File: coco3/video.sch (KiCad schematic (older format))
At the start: 67 parts, among them CN3 Conn_02x05_Odd_Even, IC36 MC78L08_TO92, J5A1001 CVIDEO, J5B1001 SOUND, Q2 2SC945(NTE85), Q3 2SC945(NTE85), Q4 MPSA13(NTE46), Q5 2SC945(NTE85), Q6 2SC945(NTE85), Q7 2SC945(NTE85), SW3 SW3

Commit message: -replaced PIA's with he PLCC44 package versions -removed RF modulator -removed DRAM
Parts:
- removed C67: 10uF 25v, Capacitor_THT:CP_Radial_D5.0mm_P2.00mm, symbol Device:CP_Small
- removed R26: 2.2K, Resistor_THT:R_Axial_DIN0207_L6.3mm_D2.5mm_P10.16mm_Horizontal, symbol Device:R_Small_US
- removed R60: 100, Resistor_THT:R_Axial_DIN0207_L6.3mm_D2.5mm_P10.16mm_Horizontal, symbol Device:R_Small_US
- removed RF1: CoCo3RFModulator, coco2:CoCo 3 RF Modulator, symbol coco2:CoCo3RFModulator
- removed SW3: SW3, coco2:SW_EG1213, symbol Switch:SW_SPDT
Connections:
- net labels removed: CH, S, V
- wire segments 195 -> 171
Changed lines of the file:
@@
 	0    -1   -1   0
-$EndComp
-Wire Wire Line
-	6650 4150 6650 4300
-Wire Wire Line
-	6400 4150 6650 4150
-Wire Wire Line
-	6400 4000 6400 4150
-$Comp
-L power:GNDS #PWR?
-U 1 1 61184351
-P 6650 4300
-AR Path="/602A51A8/61184351" Ref="#PWR?"  Part="1"
-AR Path="/60308A73/61184351" Ref="#PWR?"  Part="1"
-AR Path="/603E4732/61184351" Ref="#PWR?"  Part="1"
-AR Path="/603D345E/61184351" Ref="#PWR?"  Part="1"
-AR Path="/61184351" Ref="#PWR?"  Part="1"
-AR Path="/612A4892/61184351" Ref="#PWR01104"  Part="1"
-F 0 "#PWR01104" H 6650 4050 50  0001 C CNN
-F 1 "GNDS" H 6650 4150 50  0000 C CNN
-F 2 "" H 6650 4300 50  0001 C CNN
-F 3 "" H 6650 4300 50  0001 C CNN
-	1    6650 4300
-	1    0    0    -1
-$EndComp
-Wire Wire Line
-	6200 4450 6200 4000
-Wire Wire Line
-	6000 4450 6200 4450
-$Comp
-L Device:R_Small_US R?
-U 1 1 6116CABF
-P 5900 4450
-AR Path="/60273794/6116CABF" Ref="R?"  Part="1"
-AR Path="/603D560B/6116CABF" Ref="R?"  Part="1"
-AR Path="/603CF7B8/6116CABF" Ref="R?"  Part="1"
-AR Path="/612A4892/6116CABF" Ref="R60"  Part="1"
-F 0 "R60" V 6000 4400 50  0000 L CNN
-F 1 "100" V 5800 4400 50  0000 L CNN
-F 2 "Resistor_THT:R_Axial_DIN0207_L6.3mm_D2.5mm_P10.16mm_Horizontal" H 5900 4450 50  0001 C CNN
-F 3 " https://www.seielect.com/catalog/sei-cf_cfm.pdf" H 5900 4450 50  0001 C CNN
-F 4 "digikey" H 5900 4450 50  0001 C CNN "Vendor"
-F 5 "CF14JT100RCT-ND" H 5900 4450 50  0001 C CNN "Vendor part#"
-F 6 "CF14JT100R" H 5900 4450 50  0001 C CNN "Manufacturer part#"
-	1    5900 4450
-	0    -1   -1   0
-$EndComp
-$Comp
-L Switch:SW_SPDT SW3
-U 1 1 6113439A
-P 6300 3800
-F 0 "SW3" V 6254 3948 50  0000 L CNN
-F 1 "SW3" V 6345 3948 50  0000 L CNN
-F 2 "coco2:SW_EG1213" H 6300 3800 50  0001 C CNN
-F 3 "https://sten-eswitch-13110800-production.s3.amazonaws.com/system/asset/product_line/data_sheet/119/EG.pdf" H 6300 3800 50  0001 C CNN
-F 4 "digikey" H 6300 3800 50  0001 C CNN "Vendor"
-F 5 "EG1906-ND" H 6300 3800 50  0001 C CNN "Vendor part#"
-F 6 "EG1213" H 6300 3800 50  0001 C CNN "Manufacturer part#"
-	1    6300 3800
-	0    -1   1    0
 $EndComp
 Connection ~ 4550 4950
@@
 	1    0    0    -1
 $EndComp
-Connection ~ 4550 6400
-Wire Wire Line
-	4550 6600 4550 6400
-$Comp
-L power:GNDS #PWR?
-U 1 1 61305ADB
-P 4550 6950
-AR Path="/602A51A8/61305ADB" Ref="#PWR?"  Part="1"
-AR Path="/60308A73/61305ADB" Ref="#PWR?"  Part="1"
-AR Path="/603E4732/61305ADB" Ref="#PWR?"  Part="1"
-AR Path="/603D345E/61305ADB" Ref="#PWR?"  Part="1"
-AR Path="/61305ADB" Ref="#PWR?"  Part="1"
-AR Path="/612A4892/61305ADB" Ref="#PWR01103"  Part="1"
-F 0 "#PWR01103" H 4550 6700 50  0001 C CNN
-F 1 "GNDS" H 4550 6800 50  0000 C CNN
-F 2 "" H 4550 6950 50  0001 C CNN
-F 3 "" H 4550 6950 50  0001 C CNN
-	1    4550 6950
-	1    0    0    -1
-$EndComp
-$Comp
-L Device:R_Small_US R?
-U 1 1 61302455
-P 4550 6700
-AR Path="/60273794/61302455" Ref="R?"  Part="1"
-AR Path="/603D560B/61302455" Ref="R?"  Part="1"
-AR Path="/603CF7B8/61302455" Ref="R?"  Part="1"
-AR Path="/612A4892/61302455" Ref="R26"  Part="1"
-F 0 "R26" H 4650 6700 50  0000 L CNN
-F 1 "2.2K" H 4600 6800 50  0000 L CNN
-F 2 "Resistor_THT:R_Axial_DIN0207_L6.3mm_D2.5mm_P10.16mm_Horizontal" H 4550 6700 50  0001 C CNN
-F 3 "https://www.seielect.com/catalog/sei-cf_cfm.pdf" H 4550 6700 50  0001 C CNN
-F 4 "digikey" H 4550 6700 50  0001 C CNN "Vendor"
-F 5 "CF14JT2K20CT-ND" H 4550 6700 50  0001 C CNN "Vendor part#"
-F 6 "CF14JT2K20" H 4550 6700 50  0001 C CNN "Manufacturer part#"
-	1    4550 6700
-	-1   0    0    1
-$EndComp
-Wire Wire Line
-	3850 6400 4550 6400
-$Comp
-L Device:CP_Small C?
-U 1 1 612EE250
-P 3750 6400
-AR Path="/60273794/612EE250" Ref="C?"  Part="1"
-AR Path="/612A4892/612EE250" Ref="C67"  Part="1"
-F 0 "C67" V 4000 6400 50  0000 C CNN
-F 1 "10uF 25v" V 3850 6400 50  0000 C CNN
-F 2 "Capacitor_THT:CP_Radial_D5.0mm_P2.00mm" H 3750 6400 50  0001 C CNN
-F 3 "http://nichicon-us.com/english/products/pdfs/e-upw.pdf" H 3750 6400 50  0001 C CNN
-F 4 "digikey" V 3750 6400 50  0001 C CNN "Vendor"
-F 5 "493-1809-ND" V 3750 6400 50  0001 C CNN "Vendor part#"
-F 6 "UPW1E100MDD" V 3750 6400 50  0001 C CNN "Manufacturer part#"
-	1    3750 6400
-	0    -1   -1   0
-$EndComp
-Connection ~ 7500 2400
-Wire Wire Line
-	7500 2400 7050 2400
 Wire Wire Line
 	7550 2200 7250 2200
@@
 Wire Wire Line
 	4000 2250 3750 2250
-$Comp
-L coco2:CoCo3RFModulator RF1
-U 1 1 6110FA77
-P 7900 2950
-F 0 "RF1" H 7850 2750 50  0000 L CNN
-F 1 "CoCo3RFModulator" V 8150 2150 50  0000 L CNN
-F 2 "coco2:CoCo 3 RF Modulator" H 7900 2950 50  0001 C CNN
-F 3 "" H 7900 2950 50  0001 C CNN
-	1    7900 2950
-	1    0    0    -1
-$EndComp
-Wire Wire Line
-	4550 6800 4550 6950
-Wire Wire Line
-	4950 4450 5800 4450
 Wire Wire Line
 	4000 2250 4750 2250
-Wire Wire Line
-	4000 2250 4000 3350
-Wire Wire Line
-	4000 3350 2600 3350
-Wire Wire Line
-	2600 3350 2600 6400
-Wire Wire Line
-	2600 6400 3650 6400
-Wire Wire Line
-	7050 2400 7050 3300
-Wire Wire Line
-	7050 3300 7600 3300
-Wire Wire Line
-	6300 3400 6300 3600
-Wire Wire Line
-	6300 3400 7600 3400
-Text GLabel 7400 3500 0    50   Output ~ 0
-8V
-Wire Wire Line
-	7400 3500 7600 3500
-Wire Wire Line
-	6900 6400 6900 3600
-Wire Wire Line
-	6900 3600 7600 3600
-Wire Wire Line
-	4550 6400 6900 6400
-$Comp
-L power:GNDS #PWR?
-U 1 1 61354D89
-P 7350 3800
-AR Path="/602A51A8/61354D89" Ref="#PWR?"  Part="1"
-AR Path="/60308A73/61354D89" Ref="#PWR?"  Part="1"
-AR Path="/603E4732/61354D89" Ref="#PWR?"  Part="1"
-AR Path="/603D345E/61354D89" Ref="#PWR?"  Part="1"
-AR Path="/61354D89" Ref="#PWR?"  Part="1"
-AR Path="/612A4892/61354D89" Ref="#PWR0109"  Part="1"
-F 0 "#PWR0109" H 7350 3550 50  0001 C CNN
-F 1 "GNDS" H 7350 3650 50  0000 C CNN
-F 2 "" H 7350 3800 50  0001 C CNN
-F 3 "" H 7350 3800 50  0001 C CNN
-	1    7350 3800
-	1    0    0    -1
-$EndComp
-Wire Wire Line
-	7600 3700 7350 3700
-Wire Wire Line
-	7350 3700 7350 3800
-Text Label 7400 3300 0    50   ~ 0
-S
-Text Label 7400 3400 0    50   ~ 0
-CH
-Text Label 7450 3600 0    50   ~ 0
-V
 $EndSCHEMATC

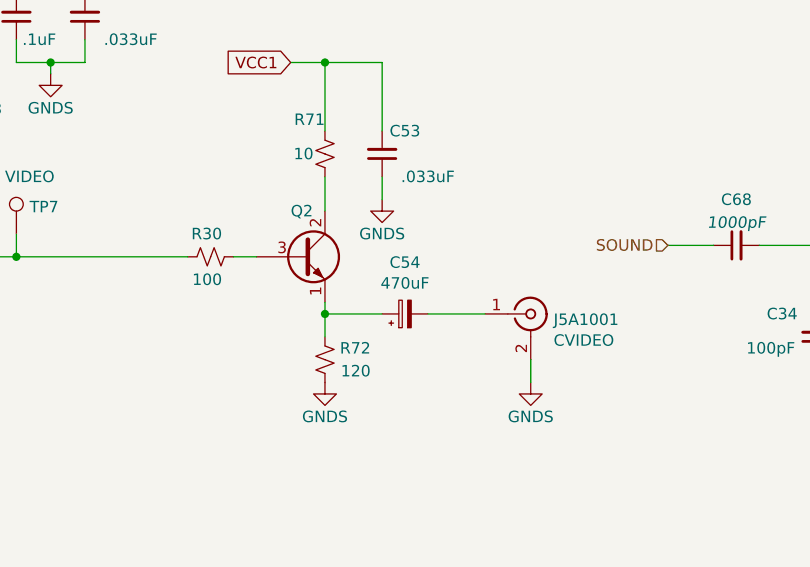
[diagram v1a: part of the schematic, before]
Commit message: -repplaced a whole bunch of THT components with SMT components
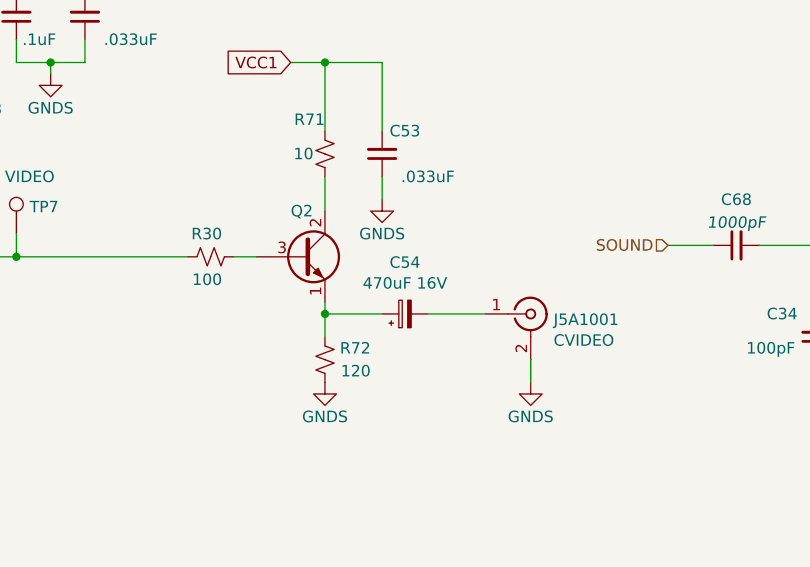
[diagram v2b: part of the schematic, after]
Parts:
- C34: footprint Capacitor_THT:C_Disc_D4.3mm_W1.9mm_P5.00mm -> Capacitor_SMD:C_0805_2012Metric_Pad1.18x1.45mm_HandSolder; Manufacturer part# K101J15C0GF5TH5 -> CL21C101JBANNNC; Vendor digikey -> JLCPCB; Vendor part# BC1042CT-ND -> C1790
- C37: footprint Capacitor_THT:C_Disc_D4.7mm_W2.5mm_P5.00mm -> Capacitor_SMD:C_0805_2012Metric_Pad1.18x1.45mm_HandSolder; Manufacturer part# K390J15C0GF5TL2 -> 0805N390J500CT; Vendor digikey -> JLCPCB; Vendor part# BC1008CT-ND -> C296098
- C42, C50, C51: footprint Capacitor_THT:C_Disc_D4.7mm_W2.5mm_P5.00mm -> Capacitor_SMD:C_0805_2012Metric_Pad1.18x1.45mm_HandSolder; Manufacturer part# FG28C0G1H103JNT06 -> CL21A106KAYNNNE; Vendor digikey -> JLCPCB; Vendor part# 445-173474-1-ND -> C15850
- C52, C53: footprint Capacitor_THT:C_Axial_L5.1mm_D3.1mm_P10.00mm_Horizontal -> Capacitor_SMD:C_0805_2012Metric_Pad1.18x1.45mm_HandSolder; Manufacturer part# C410C333K5R5TA7200 -> 0805B333K500NT; Vendor digikey -> JLCPCB; Vendor part# 399-4470-1-ND -> C1739
- C54: value 470uF -> 470uF 16V; footprint Capacitor_THT:CP_Radial_D8.0mm_P3.50mm -> Capacitor_SMD:CP_Elec_8x10; Manufacturer part# ECA-1CM471 -> VEJ471M1CTR-0810; Vendor digikey -> JLCPCB; Vendor part# P5141-ND -> C176671
- C55, C56: footprint Capacitor_THT:CP_Radial_D5.0mm_P2.00mm -> Capacitor_SMD:CP_Elec_4x5.3; Manufacturer part# UPW1E100MDD -> VE-100M1ETR-0405; Vendor digikey -> JLCPCB; Vendor part# 493-1809-ND -> C134721
- C57: footprint Capacitor_THT:C_Axial_L5.1mm_D3.1mm_P10.00mm_Horizontal -> Capacitor_SMD:C_0805_2012Metric_Pad1.18x1.45mm_HandSolder; Manufacturer part# C410C223K5R5TA7200 -> CL21B223KBANNNC; Vendor digikey -> JLCPCB; Vendor part# 399-4464-1-ND -> C1729
- C58, C59, C68: footprint Capacitor_THT:C_Disc_D4.7mm_W2.5mm_P5.00mm -> Capacitor_SMD:C_0805_2012Metric_Pad1.18x1.45mm_HandSolder; Manufacturer part# K102K10X7RF5UH5 -> CL21B102KBCNNNC; Vendor digikey -> JLCPCB; Vendor part# BC2659CT-ND -> C46653
- C62, C63: footprint Capacitor_THT:CP_Radial_D8.0mm_P3.50mm -> Capacitor_SMD:CP_Elec_8x10; Manufacturer part# ECA-1EM221 -> VEJ221M1ETR-0810; Vendor digikey -> JLCPCB; Vendor part# P5153-ND -> C134765
- R28, R39, R46, R53, R68, R71: footprint Resistor_THT:R_Axial_DIN0207_L6.3mm_D2.5mm_P10.16mm_Horizontal -> Resistor_SMD:R_1206_3216Metric_Pad1.30x1.75mm_HandSolder; Manufacturer part# CFR-25JB-52-10R -> 1206W4F100JT5E; Vendor digikey -> JLCPCB; Vendor part# 10QBK-ND -> C17903
- R30, R34, R69: footprint Resistor_THT:R_Axial_DIN0207_L6.3mm_D2.5mm_P10.16mm_Horizontal -> Resistor_SMD:R_1206_3216Metric_Pad1.30x1.75mm_HandSolder; Manufacturer part# CF14JT100R -> 1206W4F1000T5E; Vendor digikey -> JLCPCB; Vendor part# CF14JT100RCT-ND -> C17901
- R33, R35: footprint Resistor_THT:R_Axial_DIN0207_L6.3mm_D2.5mm_P10.16mm_Horizontal -> Resistor_SMD:R_1206_3216Metric_Pad1.30x1.75mm_HandSolder; Manufacturer part# CF14JT220K -> 1206W4F2203T5E; Vendor digikey -> JLCPCB; Vendor part# CF14JT220KCT-ND -> C17956
- R36, R40, R47, R54: footprint Resistor_THT:R_Axial_DIN0207_L6.3mm_D2.5mm_P10.16mm_Horizontal -> Resistor_SMD:R_1206_3216Metric_Pad1.30x1.75mm_HandSolder; Manufacturer part# CF14JT1K00 -> 1206W4F1001T5; Vendor digikey -> JLCPCB; Vendor part# CF14JT1K00CT-ND -> C4410
- R38, R45, R52: footprint Resistor_THT:R_Axial_DIN0207_L6.3mm_D2.5mm_P10.16mm_Horizontal -> Resistor_SMD:R_1206_3216Metric_Pad1.30x1.75mm_HandSolder; Manufacturer part# CFR-25JB-52-3K -> 1206W4F3001T5E; Vendor digikey -> JLCPCB; Vendor part# 3.0KQBK-ND -> C18012
- R42, R49, R56: footprint Resistor_THT:R_Axial_DIN0207_L6.3mm_D2.5mm_P10.16mm_Horizontal -> Resistor_SMD:R_1206_3216Metric_Pad1.30x1.75mm_HandSolder; Manufacturer part# RNF14FTD2K00 -> 1206W4F2001T5E; Vendor digikey -> JLCPCB; Vendor part# RNF14FTD2K00CT-ND -> C17944
- R43, R50, R57, R72: footprint Resistor_THT:R_Axial_DIN0207_L6.3mm_D2.5mm_P10.16mm_Horizontal -> Resistor_SMD:R_1206_3216Metric_Pad1.30x1.75mm_HandSolder; Manufacturer part# CF14JT120R -> 1206W4F1200T5E; Vendor digikey -> JLCPCB; Vendor part# CF14JT120RCT-ND -> C17909
- R61, R62: footprint Resistor_THT:R_Axial_DIN0207_L6.3mm_D2.5mm_P10.16mm_Horizontal -> Resistor_SMD:R_1206_3216Metric_Pad1.30x1.75mm_HandSolder; Manufacturer part# Stackpole Electronics Inc -> 1206W4F4701T5E; Vendor digikey -> JLCPCB; Vendor part# CF14JT4K70CT-ND -> C17936

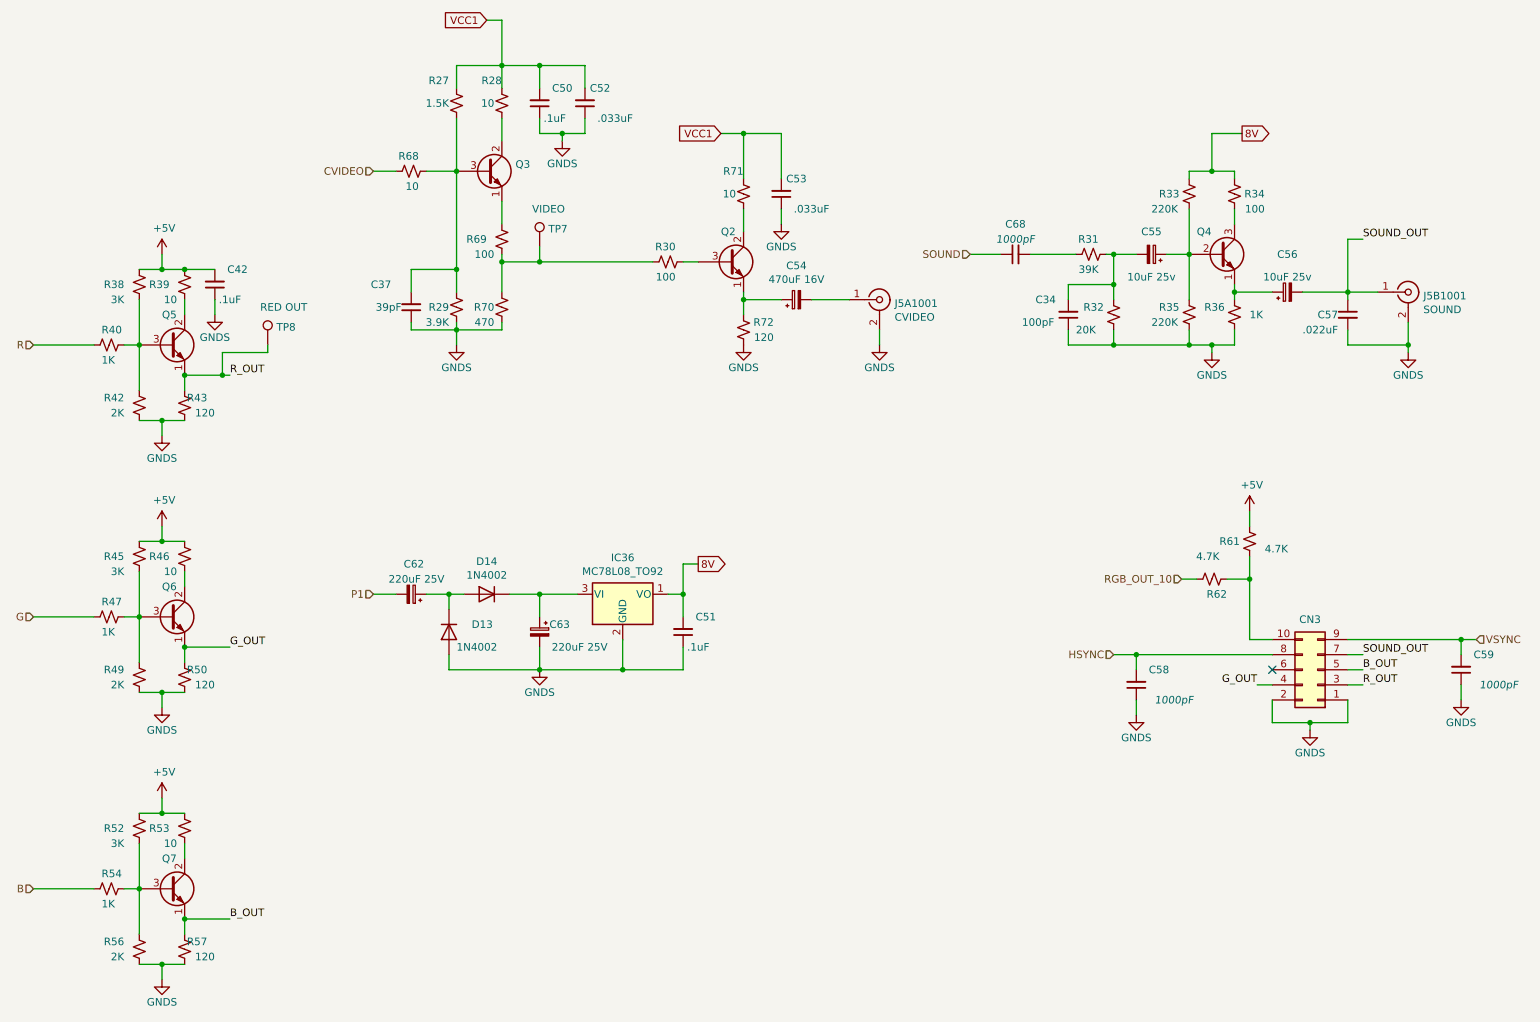
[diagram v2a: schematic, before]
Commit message: -converted more components from THT to SMD -replaced SALT chip with replacement circuitry
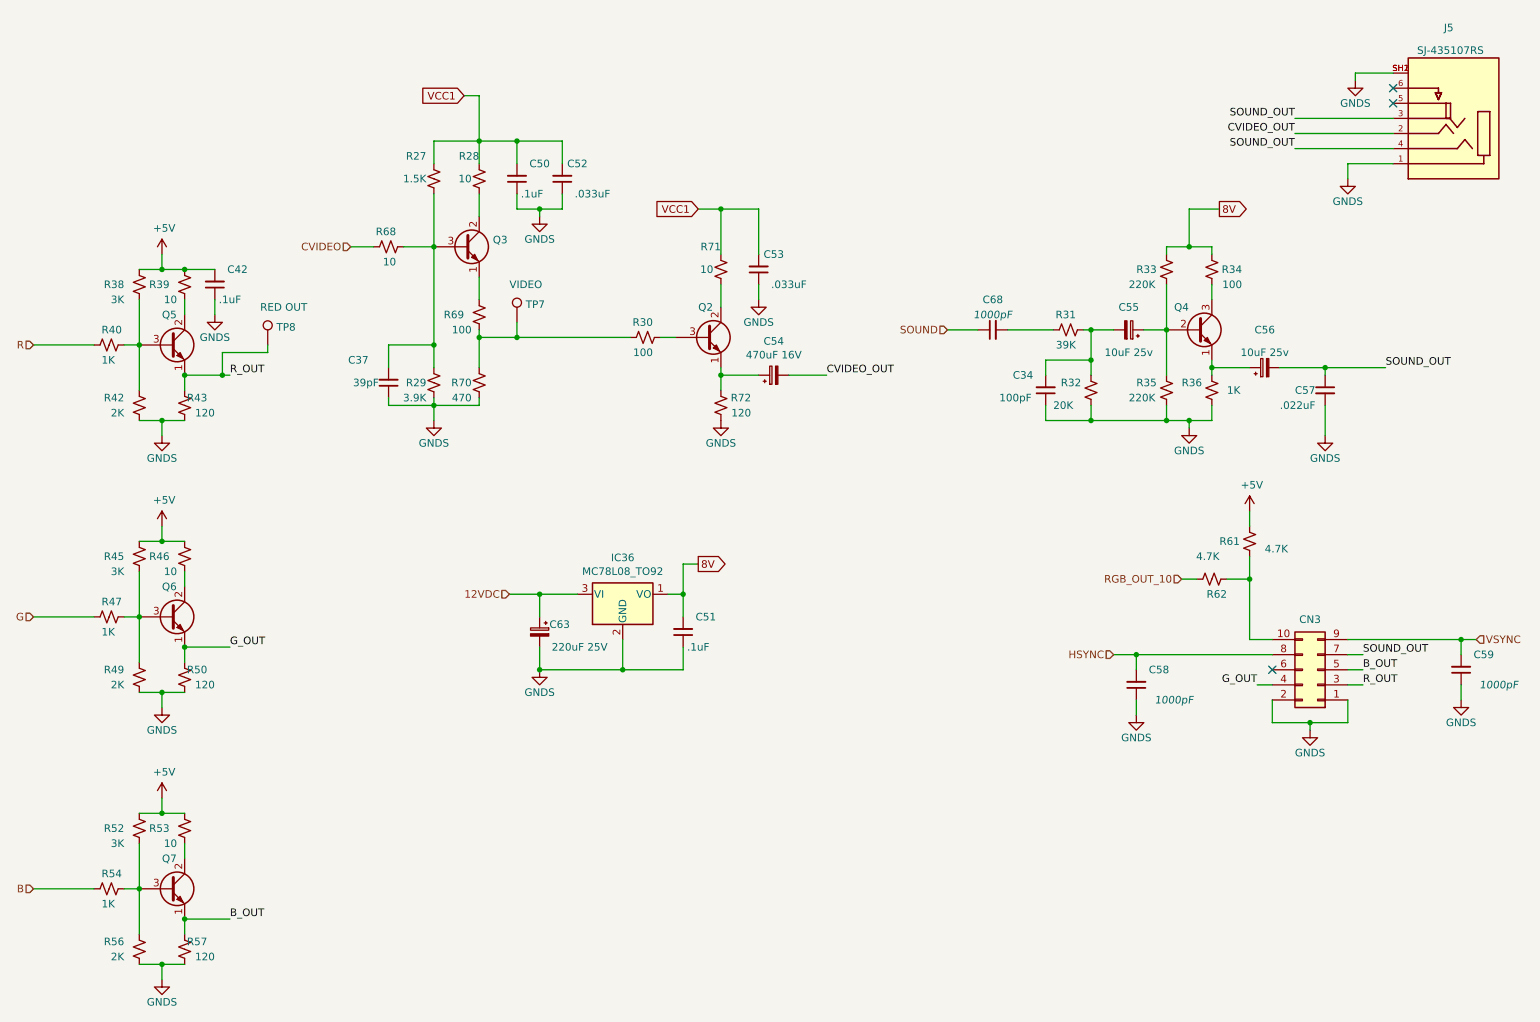
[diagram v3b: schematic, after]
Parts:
- removed C62: 220uF 25V, Capacitor_SMD:CP_Elec_8x10, symbol Device:CP_Small
- removed D13, D14: 1N4002, Diode_THT:D_DO-41_SOD81_P10.16mm_Horizontal, symbol Diode:1N4002
- removed J5A1001: CVIDEO, coco2:KLPX-0848A-2-R, symbol Connector:Conn_Coaxial
- removed J5B1001: SOUND, coco2:KLPX-0848A-2-R, symbol Connector:Conn_Coaxial
- added J5: SJ-435107RS, coco2:CUI_SJ-435107RS, symbol coco2:SJ-435107RS
- R27: footprint Resistor_THT:R_Axial_DIN0207_L6.3mm_D2.5mm_P10.16mm_Horizontal -> Resistor_SMD:R_1206_3216Metric_Pad1.30x1.75mm_HandSolder; Manufacturer part# RNF14FTD1K50 -> UNI-ROYAL(Uniroyal Elec); Vendor digikey -> JLCPCB; Vendor part# RNF14FTD1K50CT-ND -> C26030
- R29: footprint Resistor_THT:R_Axial_DIN0207_L6.3mm_D2.5mm_P10.16mm_Horizontal -> Resistor_SMD:R_1206_3216Metric_Pad1.30x1.75mm_HandSolder; Manufacturer part# CF14JT3K90 -> 1206W4F3901T5E; Vendor digikey -> JLCPCB; Vendor part# CF14JT3K90CT-ND -> C17883
- R31: footprint Resistor_THT:R_Axial_DIN0207_L6.3mm_D2.5mm_P10.16mm_Horizontal -> Resistor_SMD:R_1206_3216Metric_Pad1.30x1.75mm_HandSolder; Manufacturer part# CFR-25JB-52-39K -> 1206W4F3902T5E; Vendor digikey -> JLCPCB; Vendor part# 39KQBK-ND -> C18008
- R32: footprint Resistor_THT:R_Axial_DIN0207_L6.3mm_D2.5mm_P10.16mm_Horizontal -> Resistor_SMD:R_1206_3216Metric_Pad1.30x1.75mm_HandSolder; Manufacturer part# CFR-25JB-52-20K -> 1206W4F620KT5E; Vendor digikey -> JLCPCB; Vendor part# 20KQBK-ND -> C25344
- R70: footprint Resistor_THT:R_Axial_DIN0207_L6.3mm_D2.5mm_P10.16mm_Horizontal -> Resistor_SMD:R_1206_3216Metric_Pad1.30x1.75mm_HandSolder; Manufacturer part# CF14JT470R -> 1206W4J0471T5E; Vendor digikey -> JLCPCB; Vendor part# CF14JT470RCT-ND -> C25383
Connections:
- net GNDS: now also J5.1, J5.SH1, J5.SH2
- net SOUND_OUT: now also J5.3, J5.4
- net 12VDC: now reaches C63.1, IC36.3 (VI)
- net CVIDEO_OUT: now reaches C54.2
- net CVIDEO_OUT: now also J5.2
- no-connect marks 1 -> 3
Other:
- moved on the sheet: C34, C37, C50, C52, C53, C54, C55, C56, C57, C68, Q2, Q3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

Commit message: routed the board
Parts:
- added D1003, D1004: 1N4148, Diode_SMD:D_SOD-323F, symbol Diode:1N4148
- added J1001: RGB_2_ADAPTER_ADAPTER, Connector_PinHeader_2.54mm:PinHeader_2x03_P2.54mm_Horizontal, symbol Connector_Generic:Conn_02x03_Odd_Even
- C55, C56: value 10uF 25v -> 10uF 16v; footprint Capacitor_SMD:CP_Elec_4x5.3 -> Capacitor_Tantalum_SMD:CP_EIA-3216-18_Kemet-A; Manufacturer part# VE-100M1ETR-0405 -> TAJA106K016RNJ; Vendor part# C134721 -> C7171
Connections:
- net +5V: now also J1001.6 (Pin_6)
- net B_OUT: now also J1001.3 (Pin_3)
- net GNDS: now also J1001.1 (Pin_1)
- net G_OUT: now also J1001.4 (Pin_4)
- net HSYNC: now also D1003.2 (A)
- net R_OUT: now also J1001.5 (Pin_5)
- net VSYNC: now also D1004.2 (A)
- new net: D1003.1 (K), D1004.1 (K), J1001.2 (Pin_2)
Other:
- moved on the sheet: C51, C63, IC36
